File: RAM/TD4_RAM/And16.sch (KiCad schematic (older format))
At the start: 6 parts, among them U25 74HC21, U26 74HC21, U27 74HC21

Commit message: RAM done (damn buses\!)
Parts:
- renumbered C24 to C41, C25 to C42, C26 to C43, U25 to U42, U26 to U43, U27 to U44
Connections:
- net VCC: now also C42.1

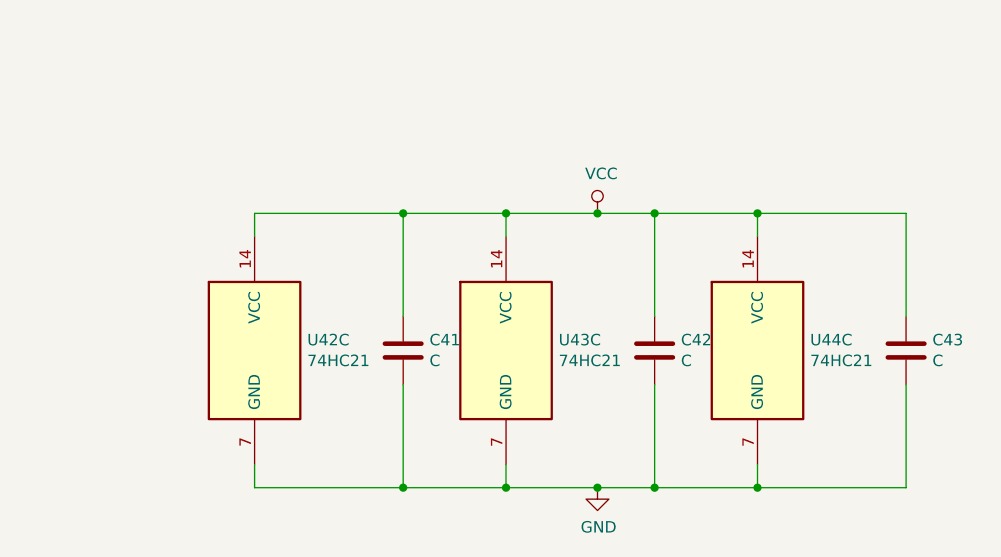
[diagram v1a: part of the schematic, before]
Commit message: Added backplane connectors to all PCBs
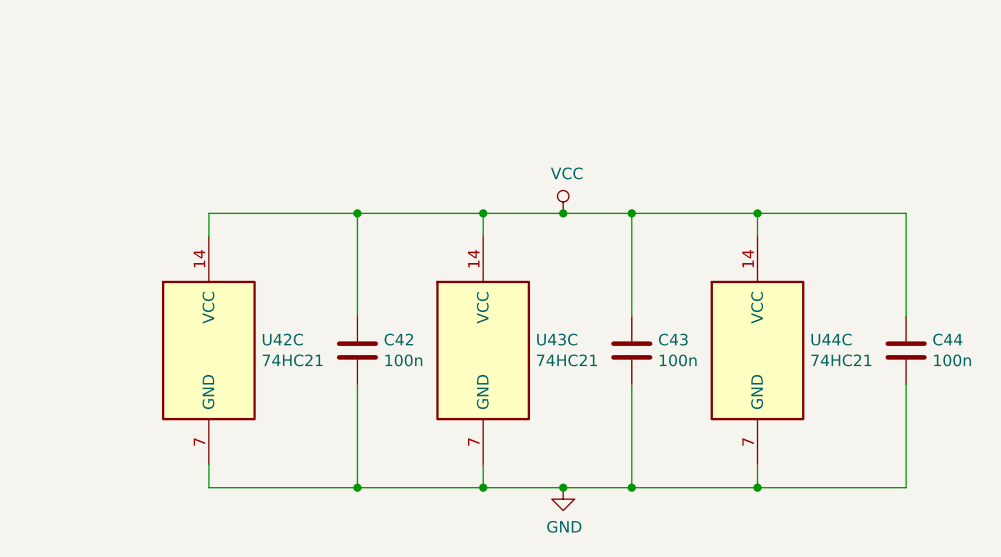
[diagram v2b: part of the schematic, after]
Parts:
- C42: renamed from C41; value C -> 100n; footprint (none) -> Capacitor_SMD:C_0805_2012Metric
- C43: renamed from C42; value C -> 100n; footprint (none) -> Capacitor_SMD:C_0805_2012Metric
- C44: renamed from C43; value C -> 100n; footprint (none) -> Capacitor_SMD:C_0805_2012Metric
- U42, U43, U44: footprint (none) -> Package_SO:SOIC-14_3.9x8.7mm_P1.27mm
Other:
- moved on the sheet: C42, C43, U42C, U43C
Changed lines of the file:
@@
 F 0 "U42" H 4900 1925 50  0000 C CNN
 F 1 "74HC21" H 4900 1834 50  0000 C CNN
-F 2 "" H 4900 1550 50  0001 C CNN
+F 2 "Package_SO:SOIC-14_3.9x8.7mm_P1.27mm" H 4900 1550 50  0001 C CNN
 F 3 "http://www.ti.com/lit/gpn/sn74LS21" H 4900 1550 50  0001 C CNN
 	1    4900 1550
@@
 F 0 "U42" H 4900 2725 50  0000 C CNN
 F 1 "74HC21" H 4900 2634 50  0000 C CNN
-F 2 "" H 4900 2350 50  0001 C CNN
+F 2 "Package_SO:SOIC-14_3.9x8.7mm_P1.27mm" H 4900 2350 50  0001 C CNN
 F 3 "http://www.ti.com/lit/gpn/sn74LS21" H 4900 2350 50  0001 C CNN
 	2    4900 2350
@@
 F 0 "U44" H 4900 3525 50  0000 C CNN
 F 1 "74HC21" H 4900 3434 50  0000 C CNN
-F 2 "" H 4900 3150 50  0001 C CNN
+F 2 "Package_SO:SOIC-14_3.9x8.7mm_P1.27mm" H 4900 3150 50  0001 C CNN
 F 3 "http://www.ti.com/lit/gpn/sn74LS21" H 4900 3150 50  0001 C CNN
 	1    4900 3150
@@
 F 0 "U43" H 4900 4325 50  0000 C CNN
 F 1 "74HC21" H 4900 4234 50  0000 C CNN
-F 2 "" H 4900 3950 50  0001 C CNN
+F 2 "Package_SO:SOIC-14_3.9x8.7mm_P1.27mm" H 4900 3950 50  0001 C CNN
 F 3 "http://www.ti.com/lit/gpn/sn74LS21" H 4900 3950 50  0001 C CNN
 	2    4900 3950
@@
 F 0 "U43" H 5800 3125 50  0000 C CNN
 F 1 "74HC21" H 5800 3034 50  0000 C CNN
-F 2 "" H 5800 2750 50  0001 C CNN
+F 2 "Package_SO:SOIC-14_3.9x8.7mm_P1.27mm" H 5800 2750 50  0001 C CNN
 F 3 "http://www.ti.com/lit/gpn/sn74LS21" H 5800 2750 50  0001 C CNN
 	1    5800 2750
@@
 L 74xx:74LS21 U?
 U 3 1 5C969F56
-P 7800 5700
+P 7600 5700
 AR Path="/5C5DC05E/5C969D73/5C969F56" Ref="U?"  Part="3"
 AR Path="/5C5DC063/5CB321B0/5C969F56" Ref="U?"  Part="3"
 AR Path="/5CBA2607/5C969F56" Ref="U42"  Part="3"
-F 0 "U42" H 8030 5746 50  0000 L CNN
-F 1 "74HC21" H 8030 5655 50  0000 L CNN
-F 2 "" H 7800 5700 50  0001 C CNN
-F 3 "http://www.ti.com/lit/gpn/sn74LS21" H 7800 5700 50  0001 C CNN
-	3    7800 5700
+F 0 "U42" H 7830 5746 50  0000 L CNN
+F 1 "74HC21" H 7830 5655 50  0000 L CNN
+F 2 "Package_SO:SOIC-14_3.9x8.7mm_P1.27mm" H 7600 5700 50  0001 C CNN
+F 3 "http://www.ti.com/lit/gpn/sn74LS21" H 7600 5700 50  0001 C CNN
+	3    7600 5700
 	1    0    0    -1
 $EndComp
@@
 L Device:C C?
 U 1 1 5C96A0AF
-P 8450 5700
+P 8250 5700
 AR Path="/5C5DC05E/5C969D73/5C96A0AF" Ref="C?"  Part="1"
 AR Path="/5C5DC063/5CB321B0/5C96A0AF" Ref="C?"  Part="1"
-AR Path="/5CBA2607/5C96A0AF" Ref="C41"  Part="1"
-F 0 "C41" H 8565 5746 50  0000 L CNN
-F 1 "C" H 8565 5655 50  0000 L CNN
-F 2 "" H 8488 5550 50  0001 C CNN
-F 3 "~" H 8450 5700 50  0001 C CNN
-	1    8450 5700
+AR Path="/5CBA2607/5C96A0AF" Ref="C42"  Part="1"
+F 0 "C42" H 8365 5746 50  0000 L CNN
+F 1 "100n" H 8365 5655 50  0000 L CNN
+F 2 "Capacitor_SMD:C_0805_2012Metric" H 8288 5550 50  0001 C CNN
+F 3 "~" H 8250 5700 50  0001 C CNN
+	1    8250 5700
 	1    0    0    -1
 $EndComp
@@
 L 74xx:74LS21 U?
 U 3 1 5C96A156
-P 8900 5700
+P 8800 5700
 AR Path="/5C5DC05E/5C969D73/5C96A156" Ref="U?"  Part="3"
 AR Path="/5C5DC063/5CB321B0/5C96A156" Ref="U?"  Part="3"
 AR Path="/5CBA2607/5C96A156" Ref="U43"  Part="3"
-F 0 "U43" H 9130 5746 50  0000 L CNN
-F 1 "74HC21" H 9130 5655 50  0000 L CNN
-F 2 "" H 8900 5700 50  0001 C CNN
-F 3 "http://www.ti.com/lit/gpn/sn74LS21" H 8900 5700 50  0001 C CNN
-	3    8900 5700
+F 0 "U43" H 9030 5746 50  0000 L CNN
+F 1 "74HC21" H 9030 5655 50  0000 L CNN
+F 2 "Package_SO:SOIC-14_3.9x8.7mm_P1.27mm" H 8800 5700 50  0001 C CNN
+F 3 "http://www.ti.com/lit/gpn/sn74LS21" H 8800 5700 50  0001 C CNN
+	3    8800 5700
 	1    0    0    -1
 $EndComp
@@
 L Device:C C?
 U 1 1 5C96A15D
-P 9550 5700
+P 9450 5700
 AR Path="/5C5DC05E/5C969D73/5C96A15D" Ref="C?"  Part="1"
 AR Path="/5C5DC063/5CB321B0/5C96A15D" Ref="C?"  Part="1"
-AR Path="/5CBA2607/5C96A15D" Ref="C42"  Part="1"
-F 0 "C42" H 9665 5746 50  0000 L CNN
-F 1 "C" H 9665 5655 50  0000 L CNN
-F 2 "" H 9588 5550 50  0001 C CNN
-F 3 "~" H 9550 5700 50  0001 C CNN
-	1    9550 5700
+AR Path="/5CBA2607/5C96A15D" Ref="C43"  Part="1"
+F 0 "C43" H 9565 5746 50  0000 L CNN
+F 1 "100n" H 9565 5655 50  0000 L CNN
+F 2 "Capacitor_SMD:C_0805_2012Metric" H 9488 5550 50  0001 C CNN
+F 3 "~" H 9450 5700 50  0001 C CNN
+	1    9450 5700
 	1    0    0    -1
 $EndComp
@@
 F 0 "U44" H 10230 5746 50  0000 L CNN
 F 1 "74HC21" H 10230 5655 50  0000 L CNN
-F 2 "" H 10000 5700 50  0001 C CNN
+F 2 "Package_SO:SOIC-14_3.9x8.7mm_P1.27mm" H 10000 5700 50  0001 C CNN
 F 3 "http://www.ti.com/lit/gpn/sn74LS21" H 10000 5700 50  0001 C CNN
 	3    10000 5700
@@
 AR Path="/5C5DC05E/5C969D73/5C96A1B2" Ref="C?"  Part="1"
 AR Path="/5C5DC063/5CB321B0/5C96A1B2" Ref="C?"  Part="1"
-AR Path="/5CBA2607/5C96A1B2" Ref="C43"  Part="1"
-F 0 "C43" H 10765 5746 50  0000 L CNN
-F 1 "C" H 10765 5655 50  0000 L CNN
-F 2 "" H 10688 5550 50  0001 C CNN
+AR Path="/5CBA2607/5C96A1B2" Ref="C44"  Part="1"
+F 0 "C44" H 10765 5746 50  0000 L CNN
+F 1 "100n" H 10765 5655 50  0000 L CNN
+F 2 "Capacitor_SMD:C_0805_2012Metric" H 10688 5550 50  0001 C CNN
 F 3 "~" H 10650 5700 50  0001 C CNN
 	1    10650 5700
@@
 F 0 "U44" H 5200 5125 50  0000 C CNN
 F 1 "74HC21" H 5200 5034 50  0000 C CNN
-F 2 "" H 5200 4750 50  0001 C CNN
+F 2 "Package_SO:SOIC-14_3.9x8.7mm_P1.27mm" H 5200 4750 50  0001 C CNN
 F 3 "http://www.ti.com/lit/gpn/sn74LS21" H 5200 4750 50  0001 C CNN
 	2    5200 4750
@@
 AR Path="/5C5DC05E/5C969D73/5C96A389" Ref="#PWR?"  Part="1"
 AR Path="/5C5DC063/5CB321B0/5C96A389" Ref="#PWR?"  Part="1"
-AR Path="/5CBA2607/5C96A389" Ref="#PWR0145"  Part="1"
-F 0 "#PWR0145" H 4800 4750 50  0001 C CNN
+AR Path="/5CBA2607/5C96A389" Ref="#PWR0160"  Part="1"
+F 0 "#PWR0160" H 4800 4750 50  0001 C CNN
 F 1 "GND" H 4805 4827 50  0000 C CNN
 F 2 "" H 4800 5000 50  0001 C CNN
@@
 L power:GND #PWR?
 U 1 1 5C96B292
-P 9300 6300
+P 9150 6300
 AR Path="/5C5DC05E/5C969D73/5C96B292" Ref="#PWR?"  Part="1"
 AR Path="/5C5DC063/5CB321B0/5C96B292" Ref="#PWR?"  Part="1"
-AR Path="/5CBA2607/5C96B292" Ref="#PWR0147"  Part="1"
-F 0 "#PWR0147" H 9300 6050 50  0001 C CNN
-F 1 "GND" H 9305 6127 50  0000 C CNN
-F 2 "" H 9300 6300 50  0001 C CNN
-F 3 "" H 9300 6300 50  0001 C CNN
-	1    9300 6300
+AR Path="/5CBA2607/5C96B292" Ref="#PWR0162"  Part="1"
+F 0 "#PWR0162" H 9150 6050 50  0001 C CNN
+F 1 "GND" H 9155 6127 50  0000 C CNN
+F 2 "" H 9150 6300 50  0001 C CNN
+F 3 "" H 9150 6300 50  0001 C CNN
+	1    9150 6300
 	1    0    0    -1
 $EndComp
@@
 L power:VCC #PWR?
 U 1 1 5C96B2ED
-P 9300 5100
+P 9150 5100
 AR Path="/5C5DC05E/5C969D73/5C96B2ED" Ref="#PWR?"  Part="1"
 AR Path="/5C5DC063/5CB321B0/5C96B2ED" Ref="#PWR?"  Part="1"
-AR Path="/5CBA2607/5C96B2ED" Ref="#PWR0146"  Part="1"
-F 0 "#PWR0146" H 9300 4950 50  0001 C CNN
-F 1 "VCC" H 9317 5273 50  0000 C CNN
-F 2 "" H 9300 5100 50  0001 C CNN
-F 3 "" H 9300 5100 50  0001 C CNN
-	1    9300 5100
-	1    0    0    -1
-$EndComp
-Wire Wire Line
-	7800 5200 7800 5100
-Wire Wire Line
-	7800 5100 8450 5100
-Wire Wire Line
-	9300 5100 9550 5100
+AR Path="/5CBA2607/5C96B2ED" Ref="#PWR0161"  Part="1"
+F 0 "#PWR0161" H 9150 4950 50  0001 C CNN
+F 1 "VCC" H 9167 5273 50  0000 C CNN
+F 2 "" H 9150 5100 50  0001 C CNN
+F 3 "" H 9150 5100 50  0001 C CNN
+	1    9150 5100
+	1    0    0    -1
+$EndComp
+Wire Wire Line
+	7600 5200 7600 5100
+Wire Wire Line
+	7600 5100 8250 5100
 Wire Wire Line
 	10650 5100 10650 5550
-Connection ~ 9300 5100
-Wire Wire Line
-	7800 6200 7800 6300
-Wire Wire Line
-	7800 6300 8450 6300
+Wire Wire Line
+	7600 6200 7600 6300
+Wire Wire Line
+	7600 6300 8250 6300
 Wire Wire Line
 	10650 6300 10650 5850
@@
 	10000 6300 10650 6300
 Wire Wire Line
-	9550 5850 9550 6300
-Connection ~ 9550 6300
-Wire Wire Line
-	9550 6300 10000 6300
-Wire Wire Line
-	9300 6300 9550 6300
-Connection ~ 9300 6300
-Wire Wire Line
-	8900 6200 8900 6300
-Connection ~ 8900 6300
-Wire Wire Line
-	8900 6300 9300 6300
-Wire Wire Line
-	8450 5850 8450 6300
-Connection ~ 8450 6300
-Wire Wire Line
-	8450 6300 8900 6300
-Wire Wire Line
-	8450 5550 8450 5100
-Connection ~ 8450 5100
-Wire Wire Line
-	8450 5100 8900 5100
-Wire Wire Line
-	8900 5200 8900 5100
-Connection ~ 8900 5100
-Wire Wire Line
-	8900 5100 9300 5100
-Connection ~ 9550 5100
-Wire Wire Line
-	9550 5100 10000 5100
+	9450 5850 9450 6300
+Connection ~ 9450 6300
+Wire Wire Line
+	9450 6300 10000 6300
+Wire Wire Line
+	8800 6200 8800 6300
+Connection ~ 8800 6300
+Wire Wire Line
+	8800 6300 9150 6300
+Wire Wire Line
+	8250 5850 8250 6300
+Connection ~ 8250 6300
+Wire Wire Line
+	8250 6300 8800 6300
+Wire Wire Line
+	8250 5550 8250 5100
+Connection ~ 8250 5100
+Wire Wire Line
+	8250 5100 8800 5100
+Wire Wire Line
+	8800 5200 8800 5100
+Connection ~ 8800 5100
+Connection ~ 9450 5100
+Wire Wire Line
+	9450 5100 10000 5100
 Wire Wire Line
 	10000 5200 10000 5100
@@
 A[0..15]
 Wire Wire Line
-	9550 5100 9550 5550
+	9450 5100 9450 5550
+Wire Wire Line
+	9150 5100 9450 5100
+Connection ~ 9150 5100
+Wire Wire Line
+	8800 5100 9150 5100
+Connection ~ 9150 6300
+Wire Wire Line
+	9150 6300 9450 6300
 Wire Bus Line
 	3200 1400 3200 3400

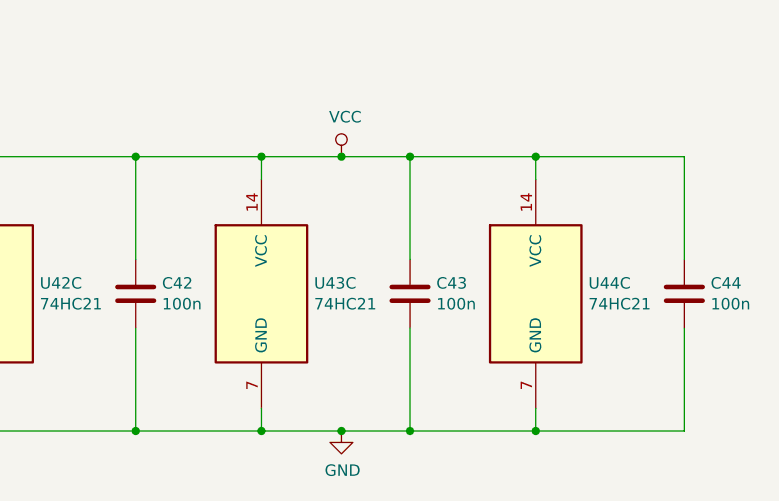
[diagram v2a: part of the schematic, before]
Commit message: Main RAM blocks routed
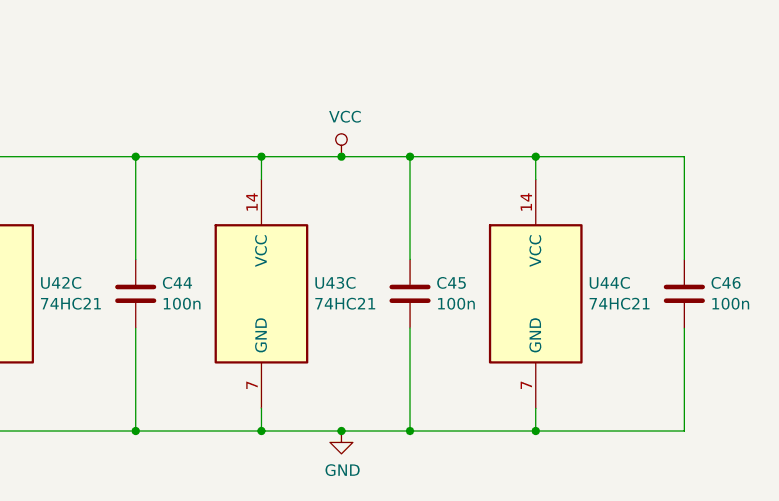
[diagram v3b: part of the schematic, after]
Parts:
- renumbered C42 to C44, C43 to C45, C44 to C46
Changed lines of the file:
@@
 AR Path="/5C5DC05E/5C969D73/5C96A0AF" Ref="C?"  Part="1"
 AR Path="/5C5DC063/5CB321B0/5C96A0AF" Ref="C?"  Part="1"
-AR Path="/5CBA2607/5C96A0AF" Ref="C42"  Part="1"
-F 0 "C42" H 8365 5746 50  0000 L CNN
+AR Path="/5CBA2607/5C96A0AF" Ref="C44"  Part="1"
+F 0 "C44" H 8365 5746 50  0000 L CNN
 F 1 "100n" H 8365 5655 50  0000 L CNN
 F 2 "Capacitor_SMD:C_0805_2012Metric" H 8288 5550 50  0001 C CNN
@@
 AR Path="/5C5DC05E/5C969D73/5C96A15D" Ref="C?"  Part="1"
 AR Path="/5C5DC063/5CB321B0/5C96A15D" Ref="C?"  Part="1"
-AR Path="/5CBA2607/5C96A15D" Ref="C43"  Part="1"
-F 0 "C43" H 9565 5746 50  0000 L CNN
+AR Path="/5CBA2607/5C96A15D" Ref="C45"  Part="1"
+F 0 "C45" H 9565 5746 50  0000 L CNN
 F 1 "100n" H 9565 5655 50  0000 L CNN
 F 2 "Capacitor_SMD:C_0805_2012Metric" H 9488 5550 50  0001 C CNN
@@
 AR Path="/5C5DC05E/5C969D73/5C96A1B2" Ref="C?"  Part="1"
 AR Path="/5C5DC063/5CB321B0/5C96A1B2" Ref="C?"  Part="1"
-AR Path="/5CBA2607/5C96A1B2" Ref="C44"  Part="1"
-F 0 "C44" H 10765 5746 50  0000 L CNN
+AR Path="/5CBA2607/5C96A1B2" Ref="C46"  Part="1"
+F 0 "C46" H 10765 5746 50  0000 L CNN
 F 1 "100n" H 10765 5655 50  0000 L CNN
 F 2 "Capacitor_SMD:C_0805_2012Metric" H 10688 5550 50  0001 C CNN
@@
 AR Path="/5C5DC05E/5C969D73/5C96A389" Ref="#PWR?"  Part="1"
 AR Path="/5C5DC063/5CB321B0/5C96A389" Ref="#PWR?"  Part="1"
-AR Path="/5CBA2607/5C96A389" Ref="#PWR0160"  Part="1"
-F 0 "#PWR0160" H 4800 4750 50  0001 C CNN
+AR Path="/5CBA2607/5C96A389" Ref="#PWR0165"  Part="1"
+F 0 "#PWR0165" H 4800 4750 50  0001 C CNN
 F 1 "GND" H 4805 4827 50  0000 C CNN
 F 2 "" H 4800 5000 50  0001 C CNN
@@
 AR Path="/5C5DC05E/5C969D73/5C96B292" Ref="#PWR?"  Part="1"
 AR Path="/5C5DC063/5CB321B0/5C96B292" Ref="#PWR?"  Part="1"
-AR Path="/5CBA2607/5C96B292" Ref="#PWR0162"  Part="1"
-F 0 "#PWR0162" H 9150 6050 50  0001 C CNN
+AR Path="/5CBA2607/5C96B292" Ref="#PWR0167"  Part="1"
+F 0 "#PWR0167" H 9150 6050 50  0001 C CNN
 F 1 "GND" H 9155 6127 50  0000 C CNN
 F 2 "" H 9150 6300 50  0001 C CNN
@@
 AR Path="/5C5DC05E/5C969D73/5C96B2ED" Ref="#PWR?"  Part="1"
 AR Path="/5C5DC063/5CB321B0/5C96B2ED" Ref="#PWR?"  Part="1"
-AR Path="/5CBA2607/5C96B2ED" Ref="#PWR0161"  Part="1"
-F 0 "#PWR0161" H 9150 4950 50  0001 C CNN
+AR Path="/5CBA2607/5C96B2ED" Ref="#PWR0166"  Part="1"
+F 0 "#PWR0166" H 9150 4950 50  0001 C CNN
 F 1 "VCC" H 9167 5273 50  0000 C CNN
 F 2 "" H 9150 5100 50  0001 C CNN

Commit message: RAM routing done
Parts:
- renumbered U44 to U43, U43 to U44
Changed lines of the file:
@@
 $Descr A4 11693 8268
 encoding utf-8
-Sheet 45 47
+Sheet 44 47
 Title ""
 Date ""
@@
 AR Path="/5C5DC05E/5C969D73/5C969E1F" Ref="U?"  Part="1"
 AR Path="/5C5DC063/5CB321B0/5C969E1F" Ref="U?"  Part="1"
-AR Path="/5CBA2607/5C969E1F" Ref="U44"  Part="1"
-F 0 "U44" H 4900 3525 50  0000 C CNN
+AR Path="/5CBA2607/5C969E1F" Ref="U43"  Part="1"
+F 0 "U43" H 4900 3525 50  0000 C CNN
 F 1 "74HC21" H 4900 3434 50  0000 C CNN
 F 2 "Package_SO:SOIC-14_3.9x8.7mm_P1.27mm" H 4900 3150 50  0001 C CNN
@@
 AR Path="/5C5DC05E/5C969D73/5C969E75" Ref="U?"  Part="1"
 AR Path="/5C5DC063/5CB321B0/5C969E75" Ref="U?"  Part="1"
-AR Path="/5CBA2607/5C969E75" Ref="U43"  Part="1"
-F 0 "U43" H 5800 3125 50  0000 C CNN
+AR Path="/5CBA2607/5C969E75" Ref="U44"  Part="1"
+F 0 "U44" H 5800 3125 50  0000 C CNN
 F 1 "74HC21" H 5800 3034 50  0000 C CNN
 F 2 "Package_SO:SOIC-14_3.9x8.7mm_P1.27mm" H 5800 2750 50  0001 C CNN
